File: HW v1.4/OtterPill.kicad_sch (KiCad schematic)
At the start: 43 parts, among them J1 USB-c, J2 VBUS, J3 1, J4 2, J5 SWD, J6 GND, J7 PAD, SW1 DFU, U1 USBLC6-4, U2 STM32F072C8Tx, U3 SY8201, U4 FUSB302BMPX

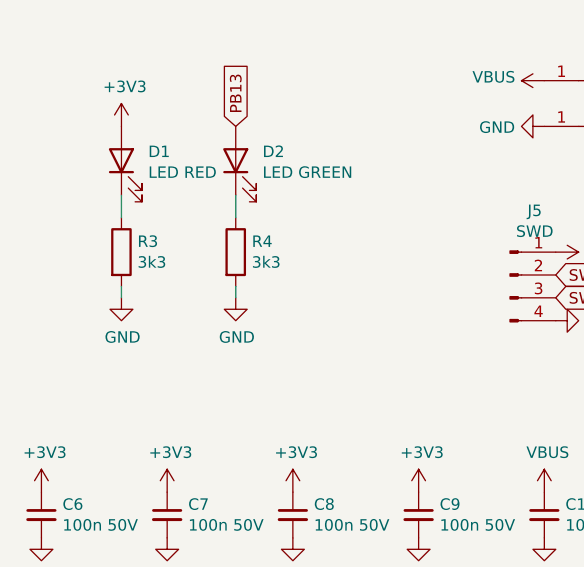
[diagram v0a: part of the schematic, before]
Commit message: fixed schematic issue
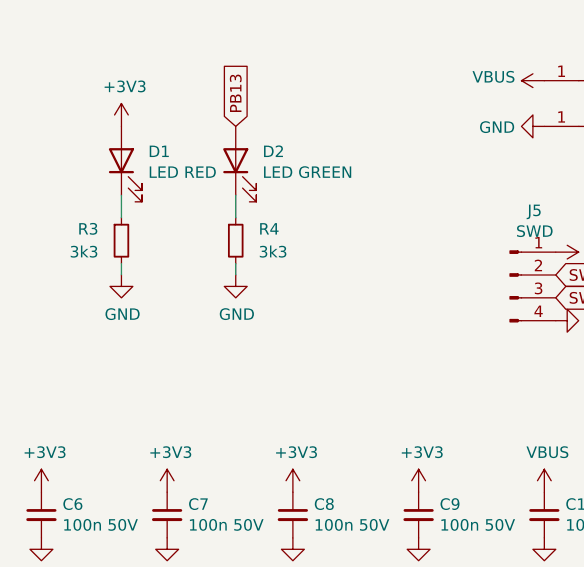
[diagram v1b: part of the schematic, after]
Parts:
- removed R3, R4: 3k3, Resistor_SMD:R_0402_1005Metric, symbol Device:R
- added R3, R4: 3k3, Resistor_SMD:R_0402_1005Metric, symbol Device:R_Small
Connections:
- net GND: now also R3.2, R4.2
- net at D1.1 (K): now also R3.1
- net at D2.1 (K): now also R4.1
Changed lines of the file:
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@@
     (stroke (width 0) (type default) (color 0 0 0 0))
   )
-  (wire (pts (xy 46.99 157.48) (xy 46.99 156.21))
+  (wire (pts (xy 46.99 154.94) (xy 46.99 153.67))
     (stroke (width 0) (type default) (color 0 0 0 0))
   )
@@
     (stroke (width 0) (type default) (color 0 0 0 0))
   )
-  (wire (pts (xy 34.29 157.48) (xy 34.29 156.21))
+  (wire (pts (xy 34.29 154.94) (xy 34.29 153.67))
     (stroke (width 0) (type default) (color 0 0 0 0))
   )
@@
     (pin "2")
   )
-  (symbol (lib_id "Device:R") (at 34.29 152.4 0) (unit 1)
-    (in_bom yes) (on_board yes)
-    (property "Reference" "R3" (id 0) (at 36.068 151.2316 0)
-      (effects (font (size 1.27 1.27)) (justify left))
-    )
-    (property "Value" "3k3" (id 1) (at 36.068 153.543 0)
-      (effects (font (size 1.27 1.27)) (justify left))
-    )
-    (property "Footprint" "Resistor_SMD:R_0402_1005Metric" (id 2) (at 32.512 152.4 90)
-      (effects (font (size 1.27 1.27)) hide)
-    )
-    (property "Datasheet" "~" (id 3) (at 34.29 152.4 0)
-      (effects (font (size 1.27 1.27)) hide)
-    )
-    (pin "1")
-    (pin "2")
-  )
-  (symbol (lib_id "Device:R") (at 46.99 152.4 0) (unit 1)
-    (in_bom yes) (on_board yes)
-    (property "Reference" "R4" (id 0) (at 48.768 151.2316 0)
-      (effects (font (size 1.27 1.27)) (justify left))
-    )
-    (property "Value" "3k3" (id 1) (at 48.768 153.543 0)
-      (effects (font (size 1.27 1.27)) (justify left))
-    )
-    (property "Footprint" "Resistor_SMD:R_0402_1005Metric" (id 2) (at 45.212 152.4 90)
-      (effects (font (size 1.27 1.27)) hide)
-    )
-    (property "Datasheet" "~" (id 3) (at 46.99 152.4 0)
-      (effects (font (size 1.27 1.27)) hide)
-    )
-    (pin "1")
-    (pin "2")
-  )
-  (symbol (lib_id "power:GND") (at 46.99 157.48 0) (unit 1)
-    (in_bom yes) (on_board yes)
-    (property "Reference" "#PWR0114" (id 0) (at 46.99 163.83 0)
-      (effects (font (size 1.27 1.27)) hide)
-    )
-    (property "Value" "GND" (id 1) (at 47.117 161.8742 0))
-    (property "Footprint" "" (id 2) (at 46.99 157.48 0)
-      (effects (font (size 1.27 1.27)) hide)
-    )
-    (property "Datasheet" "" (id 3) (at 46.99 157.48 0)
+  (symbol (lib_id "power:GND") (at 46.99 154.94 0) (unit 1)
+    (in_bom yes) (on_board yes)
+    (property "Reference" "#PWR0114" (id 0) (at 46.99 161.29 0)
+      (effects (font (size 1.27 1.27)) hide)
+    )
+    (property "Value" "GND" (id 1) (at 47.117 159.3342 0))
+    (property "Footprint" "" (id 2) (at 46.99 154.94 0)
+      (effects (font (size 1.27 1.27)) hide)
+    )
+    (property "Datasheet" "" (id 3) (at 46.99 154.94 0)
       (effects (font (size 1.27 1.27)) hide)
     )
@@
     (pin "2")
   )
-  (symbol (lib_id "power:GND") (at 34.29 157.48 0) (unit 1)
-    (in_bom yes) (on_board yes)
-    (property "Reference" "#PWR0121" (id 0) (at 34.29 163.83 0)
-      (effects (font (size 1.27 1.27)) hide)
-    )
-    (property "Value" "GND" (id 1) (at 34.417 161.8742 0))
-    (property "Footprint" "" (id 2) (at 34.29 157.48 0)
-      (effects (font (size 1.27 1.27)) hide)
-    )
-    (property "Datasheet" "" (id 3) (at 34.29 157.48 0)
+  (symbol (lib_id "power:GND") (at 34.29 154.94 0) (unit 1)
+    (in_bom yes) (on_board yes)
+    (property "Reference" "#PWR0121" (id 0) (at 34.29 161.29 0)
+      (effects (font (size 1.27 1.27)) hide)
+    )
+    (property "Value" "GND" (id 1) (at 34.417 159.3342 0))
+    (property "Footprint" "" (id 2) (at 34.29 154.94 0)
+      (effects (font (size 1.27 1.27)) hide)
+    )
+    (property "Datasheet" "" (id 3) (at 34.29 154.94 0)
       (effects (font (size 1.27 1.27)) hide)
     )
@@
     )
     (property "Datasheet" "~" (id 3) (at 171.45 27.94 0)
+      (effects (font (size 1.27 1.27)) hide)
+    )
+    (pin "1")
+    (pin "2")
+  )
+  (symbol (lib_id "Device:R_Small") (at 34.29 151.13 0) (unit 1)
+    (in_bom yes) (on_board yes) (fields_autoplaced)
+    (property "Reference" "R3" (id 0) (at 31.75 149.8599 0)
+      (effects (font (size 1.27 1.27)) (justify right))
+    )
+    (property "Value" "3k3" (id 1) (at 31.75 152.3999 0)
+      (effects (font (size 1.27 1.27)) (justify right))
+    )
+    (property "Footprint" "Resistor_SMD:R_0402_1005Metric" (id 2) (at 34.29 151.13 0)
+      (effects (font (size 1.27 1.27)) hide)
+    )
+    (property "Datasheet" "~" (id 3) (at 34.29 151.13 0)
+      (effects (font (size 1.27 1.27)) hide)
+    )
+    (pin "1")
+    (pin "2")
+  )
+  (symbol (lib_id "Device:R_Small") (at 46.99 151.13 0) (unit 1)
+    (in_bom yes) (on_board yes) (fields_autoplaced)
+    (property "Reference" "R4" (id 0) (at 49.53 149.8599 0)
+      (effects (font (size 1.27 1.27)) (justify left))
+    )
+    (property "Value" "3k3" (id 1) (at 49.53 152.3999 0)
+      (effects (font (size 1.27 1.27)) (justify left))
+    )
+    (property "Footprint" "Resistor_SMD:R_0402_1005Metric" (id 2) (at 46.99 151.13 0)
+      (effects (font (size 1.27 1.27)) hide)
+    )
+    (property "Datasheet" "~" (id 3) (at 46.99 151.13 0)
       (effects (font (size 1.27 1.27)) hide)
     )
@@
       (reference "R2") (unit 1) (value "DNP") (footprint "Resistor_SMD:R_0402_1005Metric")
     )
-    (path "/00000000-0000-0000-0000-00005cc777a1"
+    (path "/17c5b7fe-662b-4974-9d1a-80d6ebd1ea5f"
       (reference "R3") (unit 1) (value "3k3") (footprint "Resistor_SMD:R_0402_1005Metric")
     )
-    (path "/00000000-0000-0000-0000-00005cc77c43"
+    (path "/ffe97b91-751f-4d06-9859-9b4f726468e9"
       (reference "R4") (unit 1) (value "3k3") (footprint "Resistor_SMD:R_0402_1005Metric")
     )
